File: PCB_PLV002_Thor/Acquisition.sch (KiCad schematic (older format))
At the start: 62 parts, among them J10 PRESS_9, J11 PRESS_10, J12 FLAMM_1, J13 FLAMM_2, J14 TEMPRESS_1, J15 TEMPRESS_2, J16 TEMPRESS_3, J17 TEMPRESS_4, J18 TACH_1, J19 TACH_2, J2 PRESS_1, J3 PRESS_2, J4 PRESS_3, J5 PRESS_4, J6 PRESS_5, J7 PRESS_6, J8 PRESS_7, J9 PRESS_8, U10 ADC128S022, U11 ADC128S022

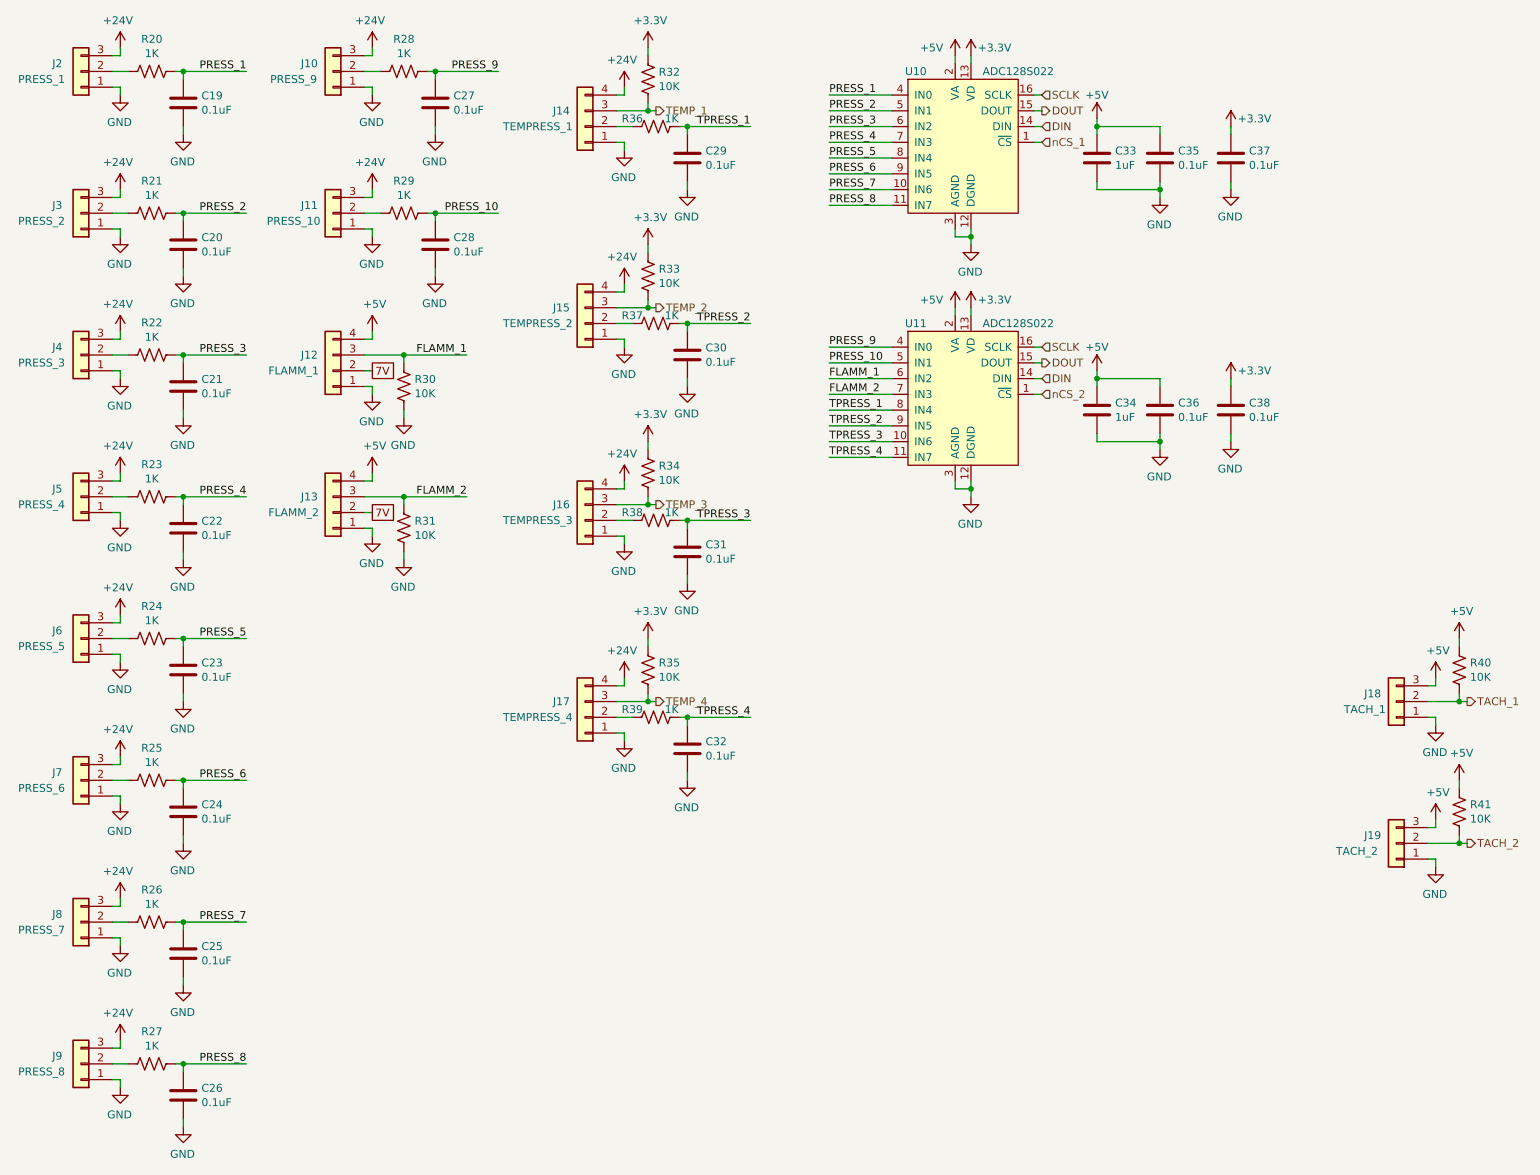
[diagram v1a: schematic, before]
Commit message: Finish schematic
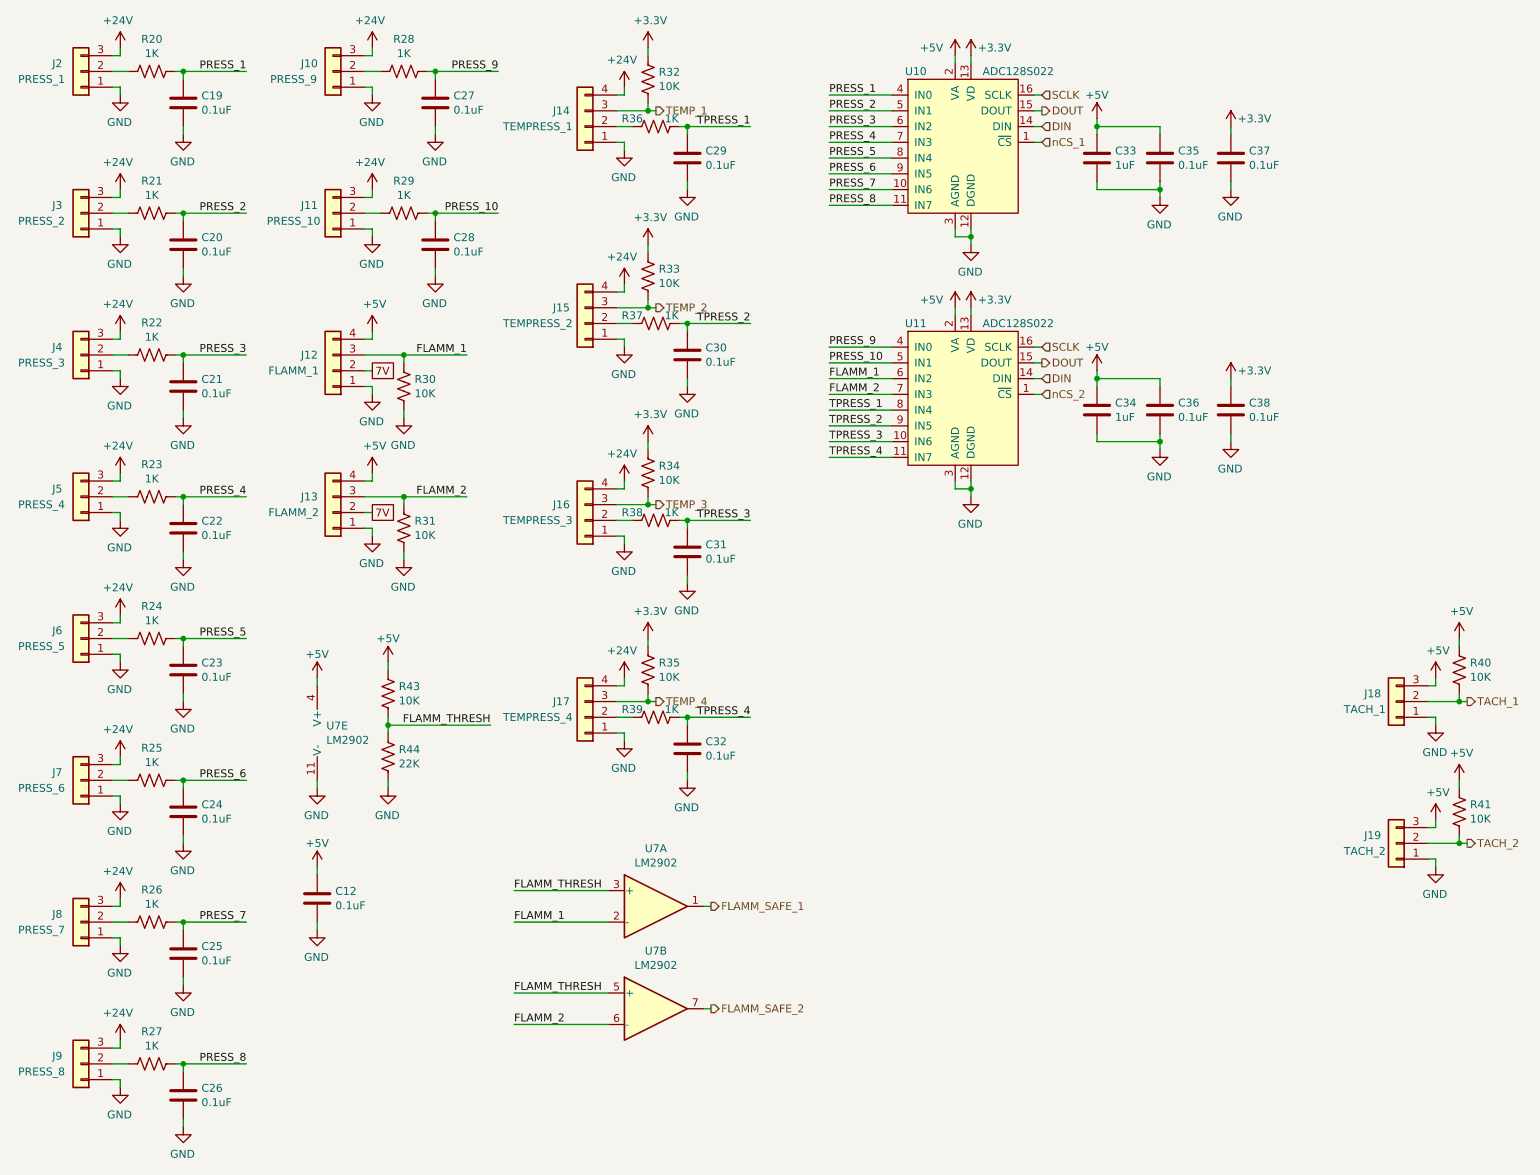
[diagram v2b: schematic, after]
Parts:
- added C12: 0.1uF, Capacitor_SMD:C_0603_1608Metric_Pad1.05x0.95mm_HandSolder, symbol Device:C
- added R43: 10K, Resistor_SMD:R_0603_1608Metric_Pad1.05x0.95mm_HandSolder, symbol Device:R_US
- added R44: 22K, Resistor_SMD:R_0603_1608Metric_Pad1.05x0.95mm_HandSolder, symbol Device:R_US
- added U7: LM2902, symbol Amplifier_Operational:LM2902
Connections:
- net +5V: now also C12.1, R43.1, U7.4 (V+)
- net FLAMM_1: now also U7.2 (-)
- net FLAMM_2: now also U7.6 (-)
- net GND: now also C12.2, R44.2, U7.11 (V-)
- new net FLAMM_SAFE_1: U7.1
- new net FLAMM_SAFE_2: U7.7
- new net FLAMM_THRESH: R43.2, R44.1, U7.3 (+), U7.5 (+)
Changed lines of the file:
@@
 EESchema Schematic File Version 4
+LIBS:PCB_PLV002_Thor-cache
 EELAYER 30 0
 EELAYER END
@@
 P 9450 5900
 F 0 "J19" H 9600 5850 50  0000 C CNN
-F 1 "TACH_2" H 9700 5950 50  0000 C CNN
+F 1 "TACH_2" H 9650 5950 50  0000 C CNN
 F 2 "" H 9450 5900 50  0001 C CNN
 F 3 "~" H 9450 5900 50  0001 C CNN
@@
 Wire Wire Line
 	8400 3300 8400 3350
+$Comp
+L Amplifier_Operational:LM2902 U7
+U 1 1 6019C49E
+P 4750 6300
+F 0 "U7" H 4750 6667 50  0000 C CNN
+F 1 "LM2902" H 4750 6576 50  0000 C CNN
+F 2 "" H 4700 6400 50  0001 C CNN
+F 3 "http://www.ti.com/lit/ds/symlink/lm2902-n.pdf" H 4800 6500 50  0001 C CNN
+	1    4750 6300
+	1    0    0    -1
+$EndComp
+Text Label 3850 6400 0    50   ~ 0
+FLAMM_1
+Wire Wire Line
+	3850 6400 4450 6400
+$Comp
+L Device:R_US R44
+U 1 1 601C9D1F
+P 3050 5350
+F 0 "R44" H 3118 5396 50  0000 L CNN
+F 1 "22K" H 3118 5305 50  0000 L CNN
+F 2 "Resistor_SMD:R_0603_1608Metric_Pad1.05x0.95mm_HandSolder" V 3090 5340 50  0001 C CNN
+F 3 "~" H 3050 5350 50  0001 C CNN
+	1    3050 5350
+	1    0    0    -1
+$EndComp
+$Comp
+L Device:R_US R43
+U 1 1 601CADBF
+P 3050 4950
+F 0 "R43" H 3118 4996 50  0000 L CNN
+F 1 "10K" H 3118 4905 50  0000 L CNN
+F 2 "Resistor_SMD:R_0603_1608Metric_Pad1.05x0.95mm_HandSolder" V 3090 4940 50  0001 C CNN
+F 3 "~" H 3050 4950 50  0001 C CNN
+	1    3050 4950
+	1    0    0    -1
+$EndComp
+Wire Wire Line
+	3050 5100 3050 5150
+Wire Wire Line
+	3050 5150 3700 5150
+Connection ~ 3050 5150
+Wire Wire Line
+	3050 5150 3050 5200
+$Comp
+L power:+5V #PWR039
+U 1 1 601FFDEC
+P 3050 4750
+F 0 "#PWR039" H 3050 4600 50  0001 C CNN
+F 1 "+5V" H 3050 4900 50  0000 C CNN
+F 2 "" H 3050 4750 50  0001 C CNN
+F 3 "" H 3050 4750 50  0001 C CNN
+	1    3050 4750
+	1    0    0    -1
+$EndComp
+Wire Wire Line
+	3050 4750 3050 4800
+$Comp
+L power:GND #PWR042
+U 1 1 60227751
+P 3050 5550
+F 0 "#PWR042" H 3050 5300 50  0001 C CNN
+F 1 "GND" H 3055 5377 50  0000 C CNN
+F 2 "" H 3050 5550 50  0001 C CNN
+F 3 "" H 3050 5550 50  0001 C CNN
+	1    3050 5550
+	-1   0    0    -1
+$EndComp
+Wire Wire Line
+	3050 5500 3050 5550
+Text Label 3700 5150 2    50   ~ 0
+FLAMM_THRESH
+Text Label 3850 6200 0    50   ~ 0
+FLAMM_THRESH
+Wire Wire Line
+	3850 6200 4450 6200
+$Comp
+L Amplifier_Operational:LM2902 U7
+U 2 1 602CC7F5
+P 4750 6950
+F 0 "U7" H 4750 7317 50  0000 C CNN
+F 1 "LM2902" H 4750 7226 50  0000 C CNN
+F 2 "" H 4700 7050 50  0001 C CNN
+F 3 "http://www.ti.com/lit/ds/symlink/lm2902-n.pdf" H 4800 7150 50  0001 C CNN
+	2    4750 6950
+	1    0    0    -1
+$EndComp
+Text Label 3850 7050 0    50   ~ 0
+FLAMM_2
+Wire Wire Line
+	3850 7050 4450 7050
+Text Label 3850 6850 0    50   ~ 0
+FLAMM_THRESH
+Wire Wire Line
+	3850 6850 4450 6850
+$Comp
+L Amplifier_Operational:LM2902 U7
+U 5 1 602EB406
+P 2700 5200
+F 0 "U7" H 2658 5246 50  0000 L CNN
+F 1 "LM2902" H 2658 5155 50  0000 L CNN
+F 2 "" H 2650 5300 50  0001 C CNN
+F 3 "http://www.ti.com/lit/ds/symlink/lm2902-n.pdf" H 2750 5400 50  0001 C CNN
+	5    2700 5200
+	1    0    0    -1
+$EndComp
+$Comp
+L power:+5V #PWR040
+U 1 1 602F01C5
+P 2600 4850
+F 0 "#PWR040" H 2600 4700 50  0001 C CNN
+F 1 "+5V" H 2600 5000 50  0000 C CNN
+F 2 "" H 2600 4850 50  0001 C CNN
+F 3 "" H 2600 4850 50  0001 C CNN
+	1    2600 4850
+	1    0    0    -1
+$EndComp
+Wire Wire Line
+	2600 4850 2600 4900
+Wire Wire Line
+	2600 5500 2600 5550
+$Comp
+L power:GND #PWR041
+U 1 1 6030D728
+P 2600 5550
+F 0 "#PWR041" H 2600 5300 50  0001 C CNN
+F 1 "GND" H 2605 5377 50  0000 C CNN
+F 2 "" H 2600 5550 50  0001 C CNN
+F 3 "" H 2600 5550 50  0001 C CNN
+	1    2600 5550
+	-1   0    0    -1
+$EndComp
+Wire Wire Line
+	2600 6400 2600 6450
+$Comp
+L power:GND #PWR044
+U 1 1 60337E3C
+P 2600 6450
+F 0 "#PWR044" H 2600 6200 50  0001 C CNN
+F 1 "GND" H 2605 6277 50  0000 C CNN
+F 2 "" H 2600 6450 50  0001 C CNN
+F 3 "" H 2600 6450 50  0001 C CNN
+	1    2600 6450
+	-1   0    0    -1
+$EndComp
+Wire Wire Line
+	2600 6050 2600 6100
+$Comp
+L Device:C C12
+U 1 1 60337E48
+P 2600 6250
+F 0 "C12" H 2715 6296 50  0000 L CNN
+F 1 "0.1uF" H 2715 6205 50  0000 L CNN
+F 2 "Capacitor_SMD:C_0603_1608Metric_Pad1.05x0.95mm_HandSolder" H 2638 6100 50  0001 C CNN
+F 3 "https://www.yageo.com/upload/media/product/productsearch/datasheet/mlcc/UPY-GPHC_X7R_6.3V-to-50V_18.pdf" H 2600 6250 50  0001 C CNN
+F 4 "CC0603KRX7R8BB104" H 850 550 50  0001 C CNN "MFPN"
+	1    2600 6250
+	1    0    0    -1
+$EndComp
+$Comp
+L power:+5V #PWR043
+U 1 1 60348105
+P 2600 6050
+F 0 "#PWR043" H 2600 5900 50  0001 C CNN
+F 1 "+5V" H 2600 6200 50  0000 C CNN
+F 2 "" H 2600 6050 50  0001 C CNN
+F 3 "" H 2600 6050 50  0001 C CNN
+	1    2600 6050
+	1    0    0    -1
+$EndComp
+Wire Wire Line
+	5100 6300 5050 6300
+Wire Wire Line
+	5050 6950 5100 6950
+Text HLabel 5100 6300 2    50   Output ~ 0
+FLAMM_SAFE_1
+Text HLabel 5100 6950 2    50   Output ~ 0
+FLAMM_SAFE_2
 $EndSCHEMATC

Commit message: Done
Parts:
- J10, J11, J2, J3, J4, J5, J6, J7, J8, J9: footprint (none) -> Connector_Molex:Molex_Nano-Fit_105313-xx03_1x03_P2.50mm_Horizontal
- J12, J13, J14, J15, J16, J17: footprint (none) -> Connector_Molex:Molex_Micro-Fit_3.0_43045-0400_2x02_P3.00mm_Horizontal
- J18, J19: footprint (none) -> Connector_Molex:Molex_Micro-Fit_3.0_43650-0300_1x03_P3.00mm_Horizontal
- U10: renamed from U7; footprint (none) -> Package_SO:SOIC-14_3.9x8.7mm_P1.27mm
- renumbered C12 to C27, C27 to C28, C28 to C29, C29 to C30, C30 to C31, C31 to C32, C32 to C33, C33 to C34, C34 to C35, C35 to C36, C36 to C37, C37 to C38, C38 to C39, R20 to R24, R21 to R25, R22 to R26, R23 to R27, R24 to R28, R25 to R29, R26 to R30, R27 to R31, R43 to R32, R44 to R33, R28 to R34, R29 to R35, R30 to R36, R31 to R37, R32 to R38, R33 to R39, R34 to R40, R35 to R41, R36 to R42, R37 to R43, R38 to R44, R39 to R45, R40 to R46, R41 to R47, U10 to U11, U11 to U12

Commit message: Schematic fix of actuator drivers
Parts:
- U11, U12: symbol boringlib:ADC128S022 -> PCB_PLV002_Thor-rescue:ADC128S022-boringlib
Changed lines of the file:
@@
 EESchema Schematic File Version 4
-LIBS:PCB_PLV002_Thor-cache
-EELAYER 29 0
+EELAYER 30 0
 EELAYER END
 $Descr USLetter 11000 8500
@@
 $EndComp
 $Comp
-L boringlib:ADC128S022 U11
+L PCB_PLV002_Thor-rescue:ADC128S022-boringlib U11
 U 1 1 6012E545
 P 6700 1300
@@
 $EndComp
 $Comp
-L boringlib:ADC128S022 U12
+L PCB_PLV002_Thor-rescue:ADC128S022-boringlib U12
 U 1 1 603A2480
 P 6700 2900
